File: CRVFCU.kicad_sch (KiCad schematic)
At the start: 154 parts, among them J1 TagConnect_TC2030, J2 Conn_01x02, J3 USB_C_Receptacle_USB2.0_16P, J4 Micro_SD_Card_Det2, J5 Conn_01x02, Q3 DMG2301L, Q4 BC818, Q5 DMG2301L, Q6 DMG2301L, U1 MS5611-01BA, U10 W25Q128JVS, U11 EClamp2515K, U12 ESDALC6V1W5, U13 USBLC6-2SC6, U14 USBLC6-2SC6, U15 MAX17049, U16 SI7232DN-T1, U17 SN74LV1T34DCK, U2 STM32H747IITx, U3 LIS2MDL, U4 ICM-45686, U5 FXMA108, U6 AP1117-50, U7 AP1117-33, U8 SI7232DN-T1, U9 USBLC6-4SC6, Y1 ECS-.327-6-34QCS-TR, Y2 ECS-250-10-33B-CKY-TR3, Y3 32.768khz

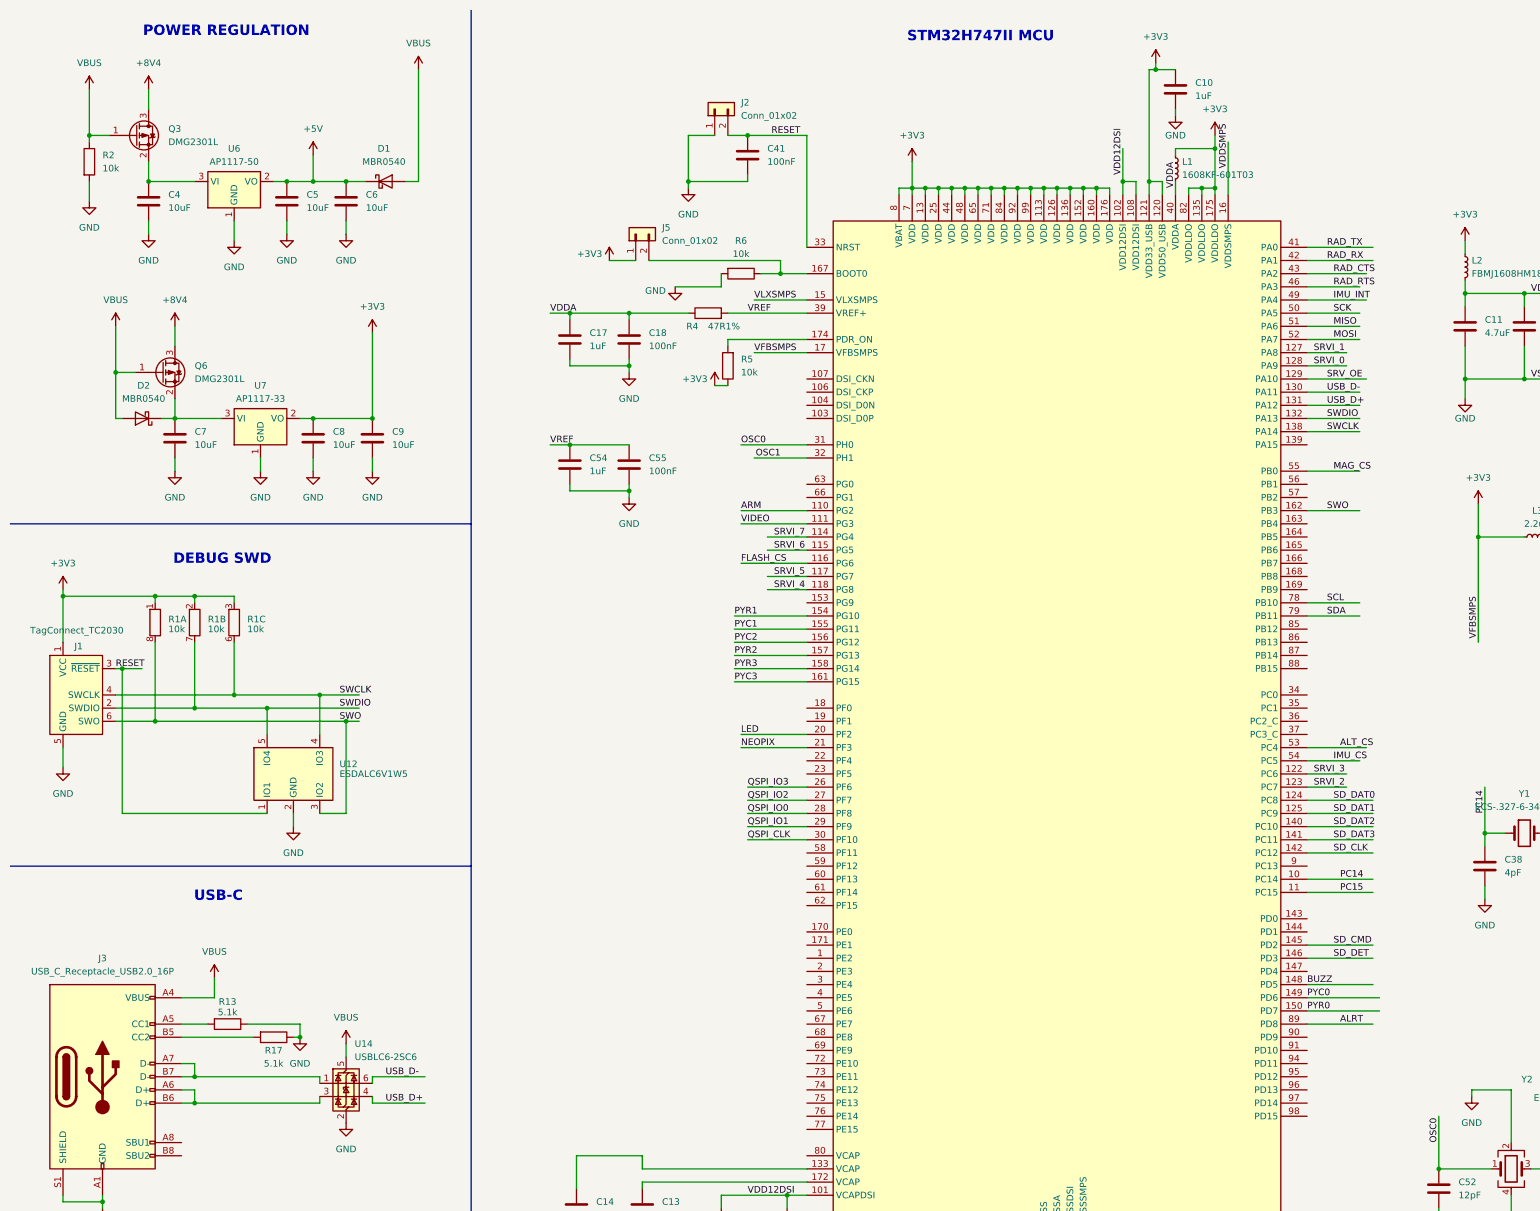
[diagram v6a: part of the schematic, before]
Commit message: ensured all servo pins are PWM capable, and changed 5v LDO to buck
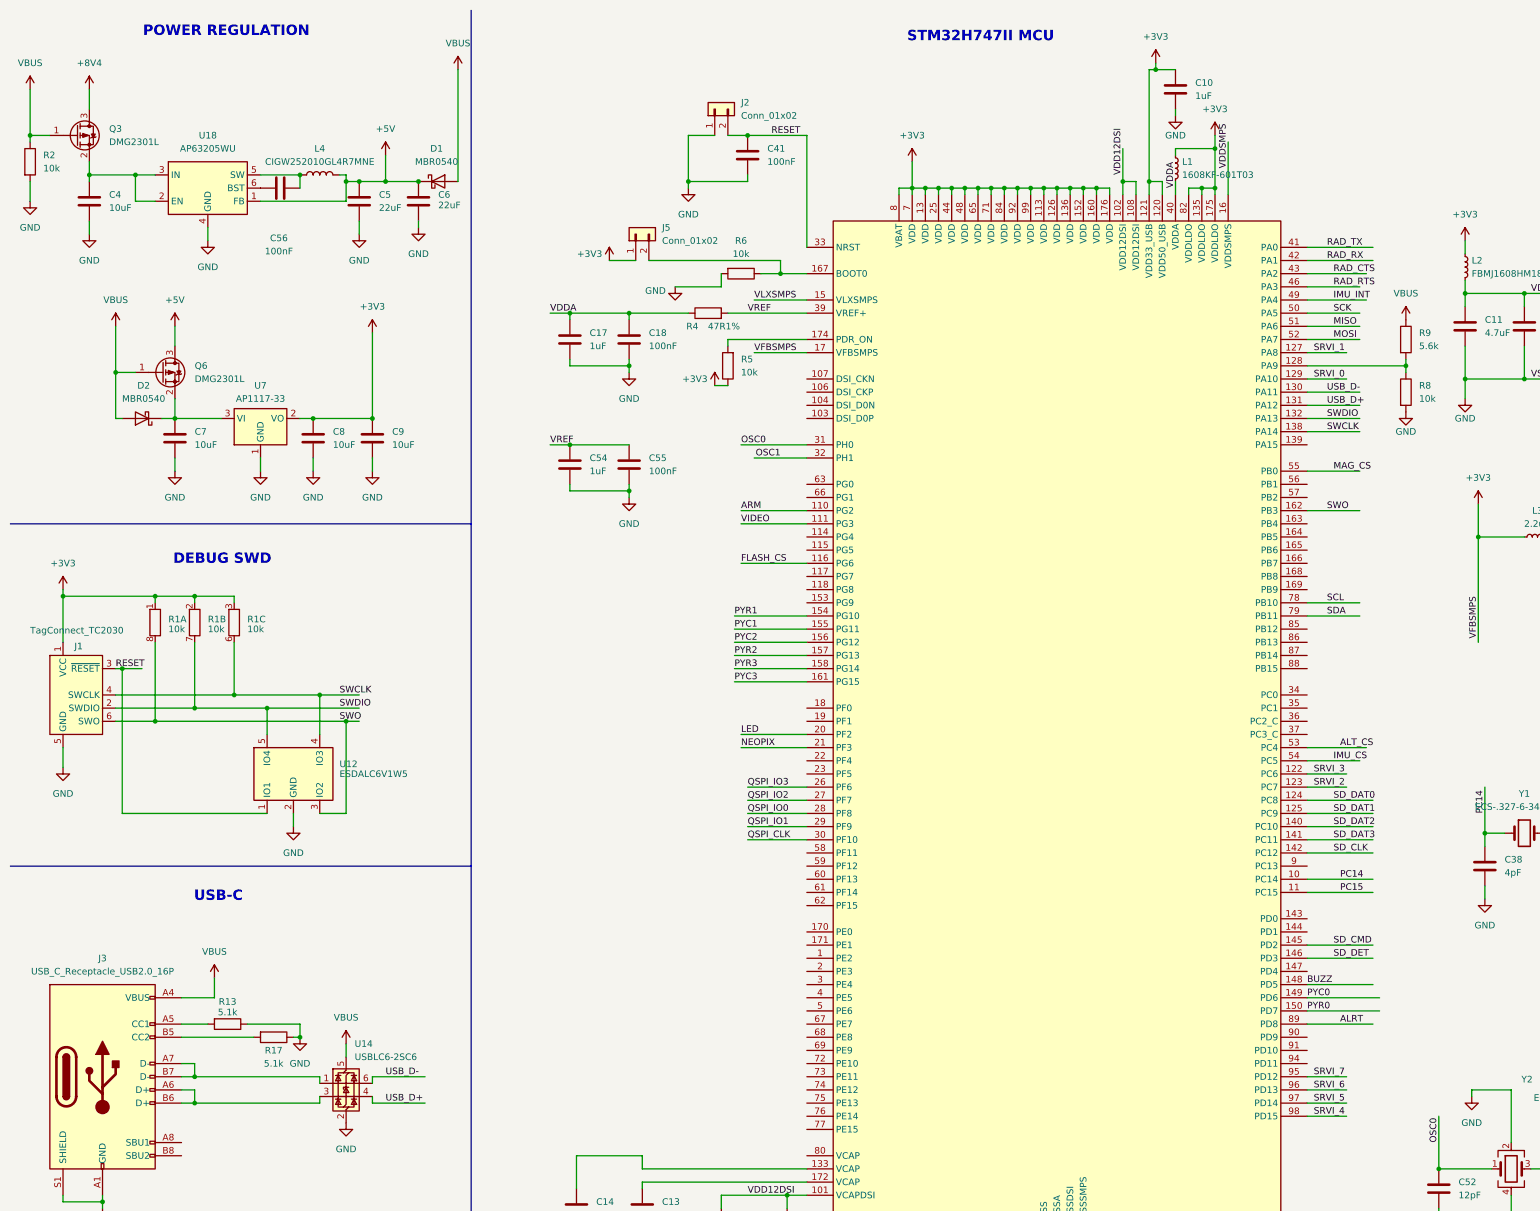
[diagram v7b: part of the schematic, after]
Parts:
- removed U6: AP1117-50, Package_TO_SOT_SMD:SOT-223-3_TabPin2, symbol Regulator_Linear:AP1117-50
- added C56: 100nF, Capacitor_SMD:C_0402_1005Metric, symbol Device:C
- added L4: CIGW252010GL4R7MNE, Inductor_SMD:L_1008_2520Metric, symbol Device:L
- added R8: 10k, Resistor_SMD:R_0402_1005Metric, symbol Device:R
- added R9: 5.6k, Resistor_SMD:R_0402_1005Metric, symbol Device:R
- added U18: AP63205WU, Package_TO_SOT_SMD:TSOT-23-6, symbol Regulator_Switching:AP63205WU
- C5, C6: value 10uF -> 22uF
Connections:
- net +5V: now also Q6.3 (D), L4.2, U18.1 (FB)
- net +8V4: no longer Q6.3 (D)
- net GND: now also R8.2, U18.4 (GND)
- net SRVI_0: now also U2.129 (PA10); no longer U2.128 (PA9)
- net SRVI_4: now also U2.98 (PD15); no longer U2.118 (PG8)
- net SRVI_5: now also U2.97 (PD14); no longer U2.117 (PG7)
- net SRVI_6: now also U2.96 (PD13); no longer U2.115 (PG5)
- net SRVI_7: now also U2.95 (PD12); no longer U2.114 (PG4)
- net SRV_OE: no longer U2.129 (PA10)
- net VBUS: now also R9.1
- net at C4.1, Q3.2 (S): now also U18.2 (EN), U18.3 (IN)
- new net: C56.2, L4.1, U18.5 (SW)
- new net: C56.1, U18.6 (BST)
- new net: R8.1, R9.2, U2.128 (PA9)
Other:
- moved on the sheet: C4, C5, C6, D1, Q3, R2

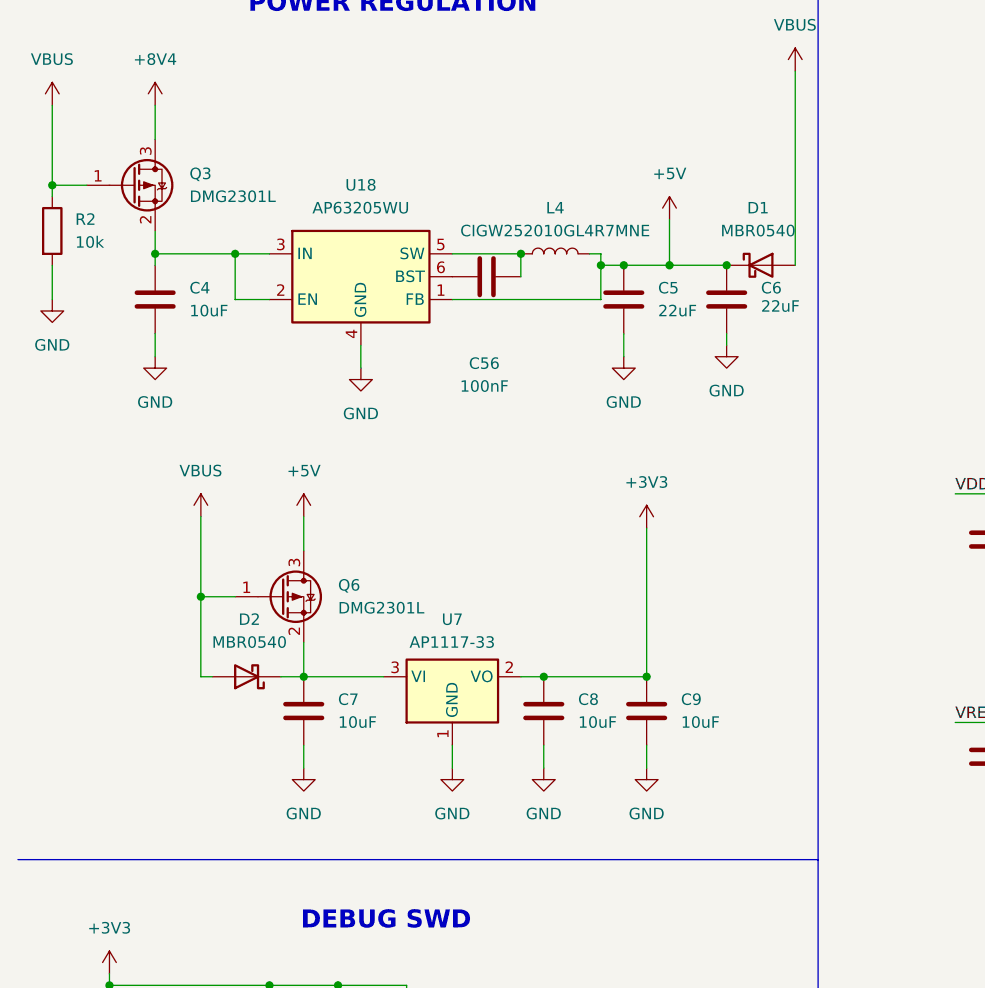
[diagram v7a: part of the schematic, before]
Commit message: added protection diode for buck and changed routing for thermal considerations
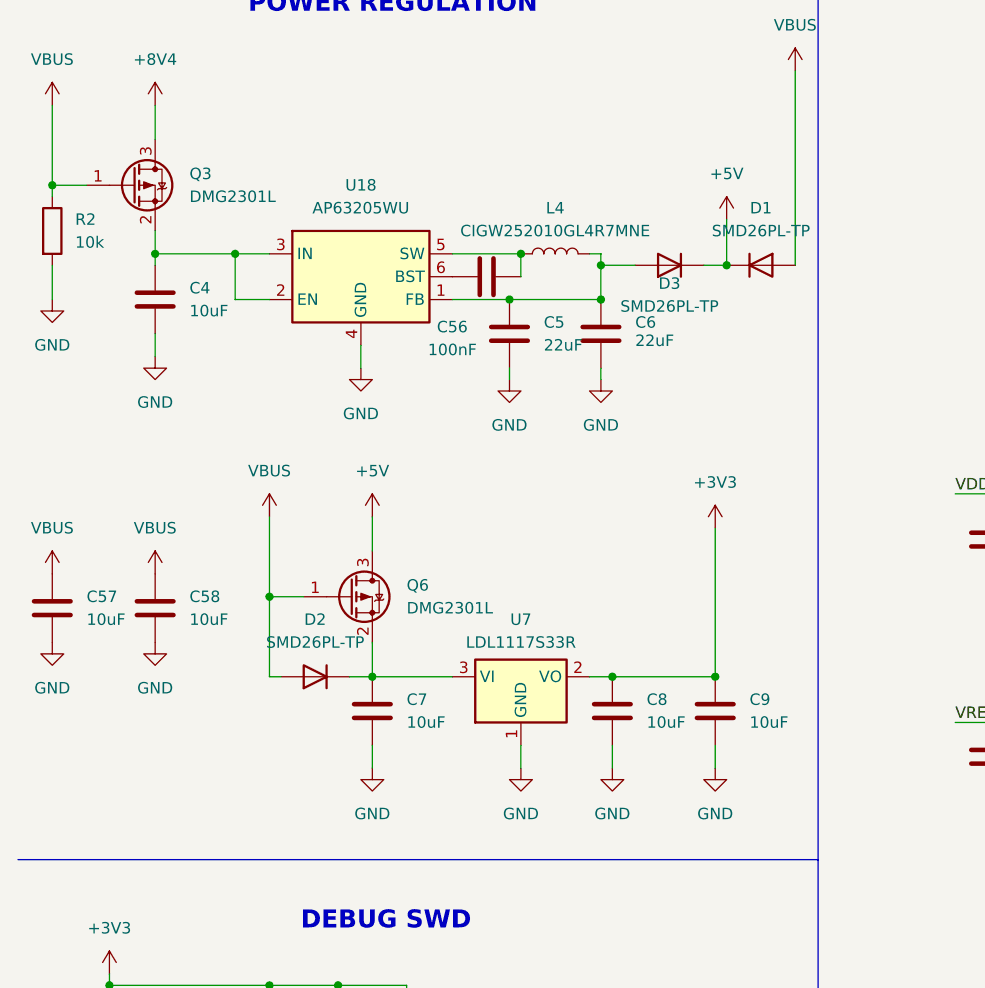
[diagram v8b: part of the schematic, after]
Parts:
- removed D1, D2: MBR0540, Diode_SMD:D_SOD-123, symbol Diode:MBR0540
- added C57, C58: 10uF, Capacitor_SMD:C_0402_1005Metric, symbol Device:C
- added D1, D2, D3: SMD26PL-TP, Diode_SMD:D_SOD-123F, symbol Device:D
- U7: value AP1117-33 -> LDL1117S33R
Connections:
- net +5V: now also D1.1 (K), D3.1 (K); no longer C5.1, C6.1, L4.2, U18.1 (FB)
- net GND: now also C57.2, C58.2
- net VBUS: now also C57.1, C58.1, D1.2 (A), D2.2 (A)
- net at C7.1, Q6.2 (S), U7.3 (VI): now also D2.1 (K)
- new net: C5.1, C6.1, D3.2 (A), L4.2, U18.1 (FB)
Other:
- moved on the sheet: C5, C6, C7, C8, C9, Q6, U7
